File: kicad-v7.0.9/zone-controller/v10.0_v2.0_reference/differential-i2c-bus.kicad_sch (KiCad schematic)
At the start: 35 parts, among them J16 1x4_idc_lsa, J17 54601-908WPLF, J18 1x4_idc_lsa, P10 1x2_pin_header, P11 1x2_pin_header, P12 1x2_pin_header, P13 1x2_pin_header, P14 1x2_pin_header, P15 1x2_pin_header, P16 1x2_pin_header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

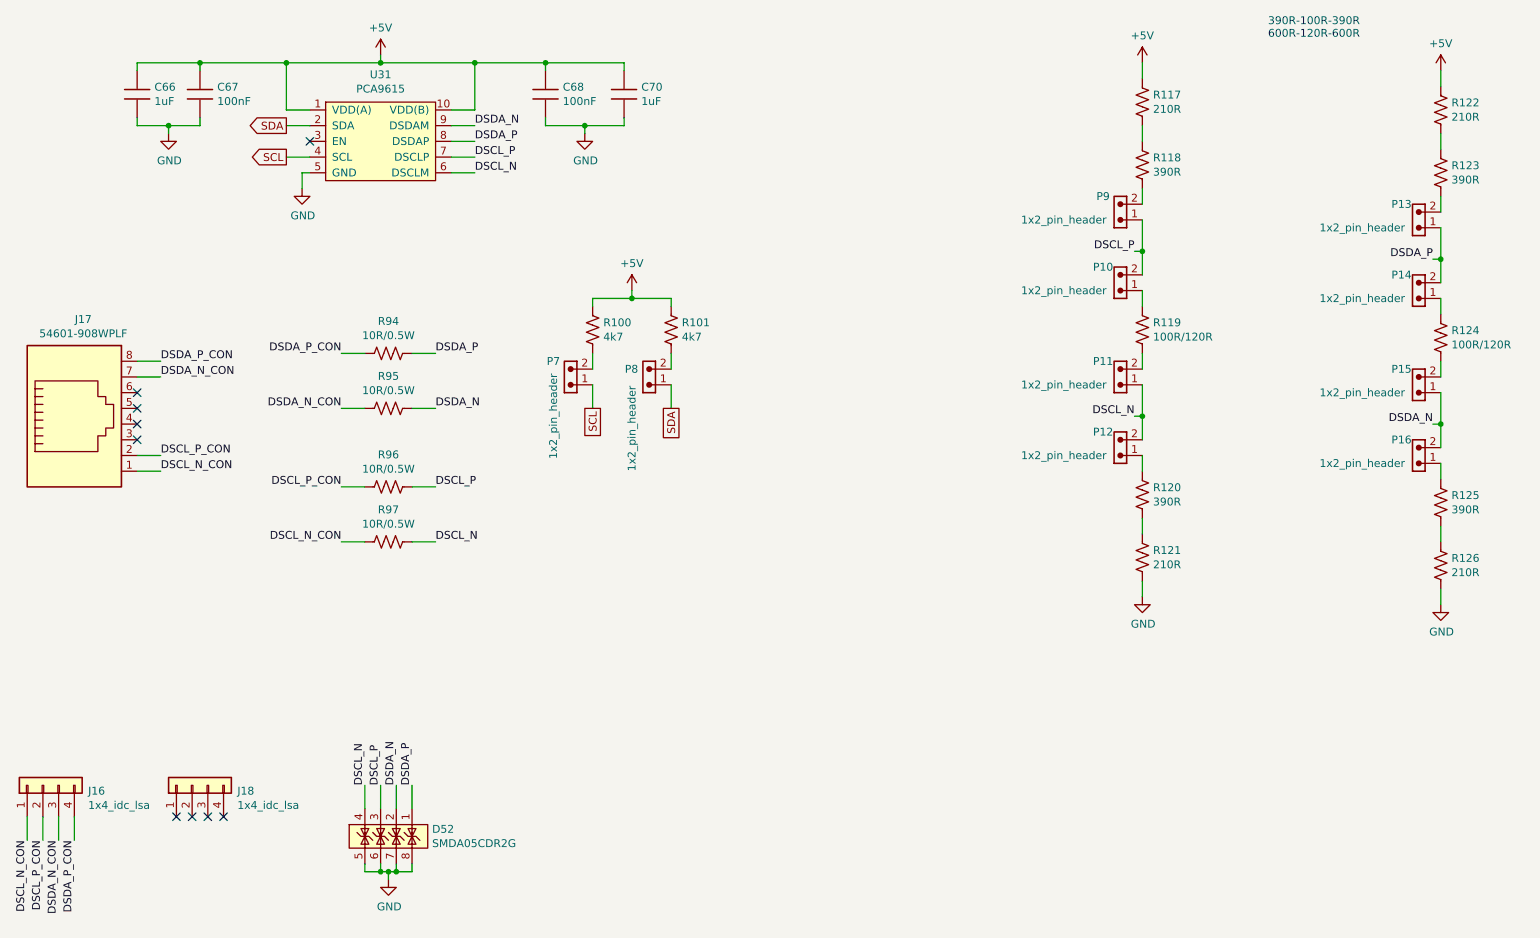
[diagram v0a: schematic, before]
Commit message: Zone controller. Change library. Small changes in schematic a PCB.
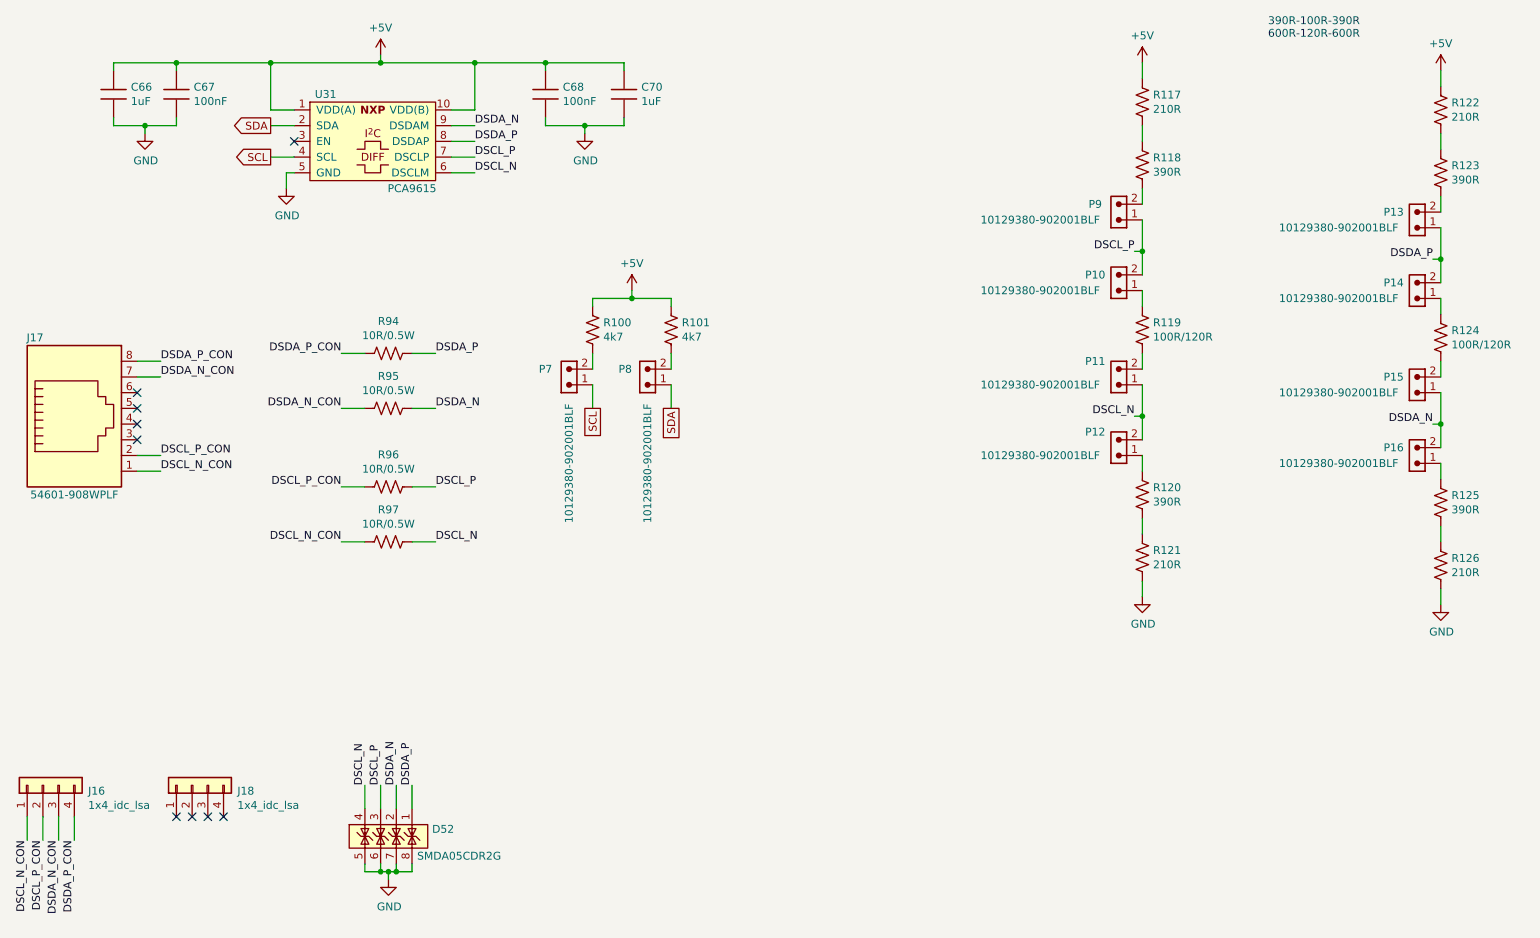
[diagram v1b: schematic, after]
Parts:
- C66, C67, C68, C70: symbol passive_component_rl:capacitor -> capacitor_smd_rl:c_1206
- D52: symbol diode_rl:SMDA05CDR2G -> transil_diode_smd_rl:SMDA05CDR2G
- J17: symbol connector_rl:rj45 -> connector_rj45_tht_rl:54601-908WPLF
- P10, P11, P12, P13, P14, P15, P16, P7, P8, P9: value 1x2_pin_header -> 10129380-902001BLF; symbol connector_rl:1x2_pin_header -> connector_smd_pin_header_2.54mm_rl:10129380-902001BLF
- R100, R101, R117, R118, R119, R120, R121, R122, R123, R124, R125, R126, R94, R95, R96, R97: symbol passive_component_rl:resistor_us -> resistor_smd_rl:r_1206_us
- U31: Manufacture NXP Semiconductors -> (none); Manufacturer (none) -> NXP Semiconductors
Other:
- moved on the sheet: C66, C67
